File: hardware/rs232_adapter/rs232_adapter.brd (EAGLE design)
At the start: 53.3 x 36.5 mm, 9 parts, among them IC1 MAX202ECWE

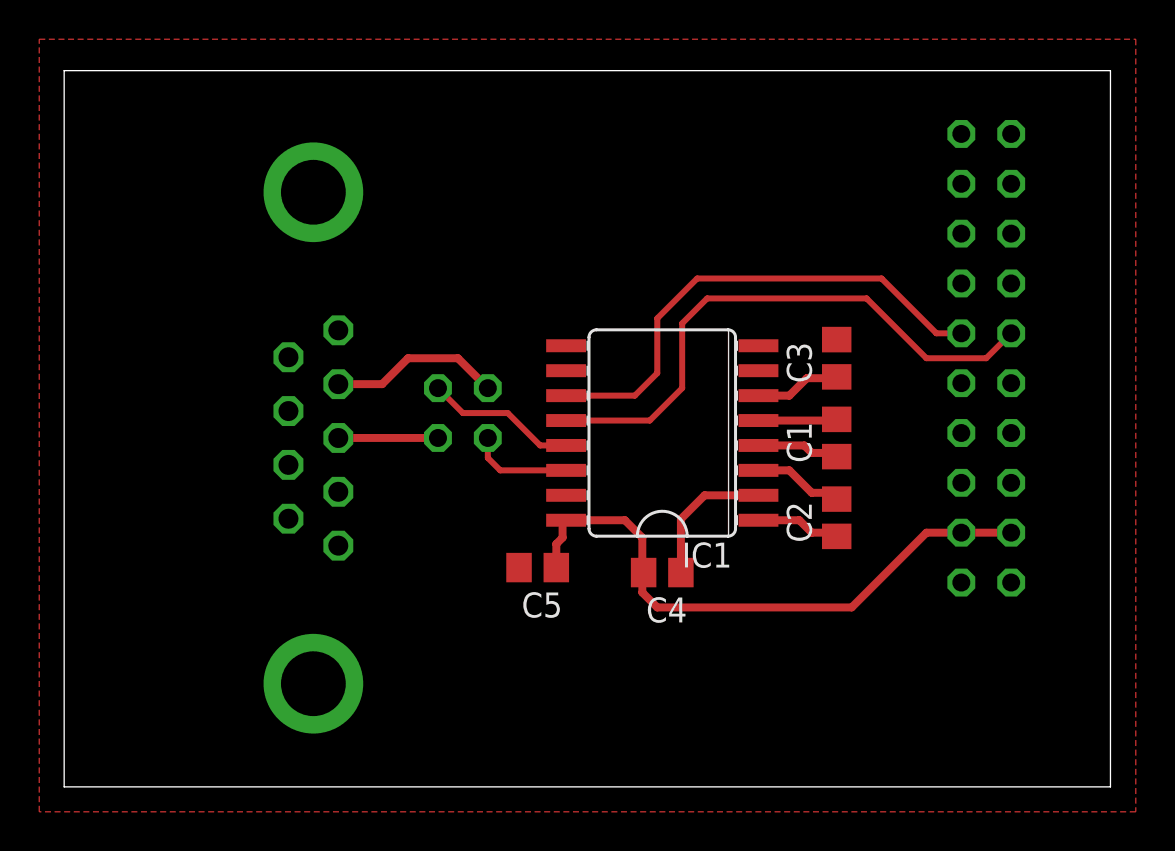
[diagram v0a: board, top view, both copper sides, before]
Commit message: change the package of the max202 and add some documentation
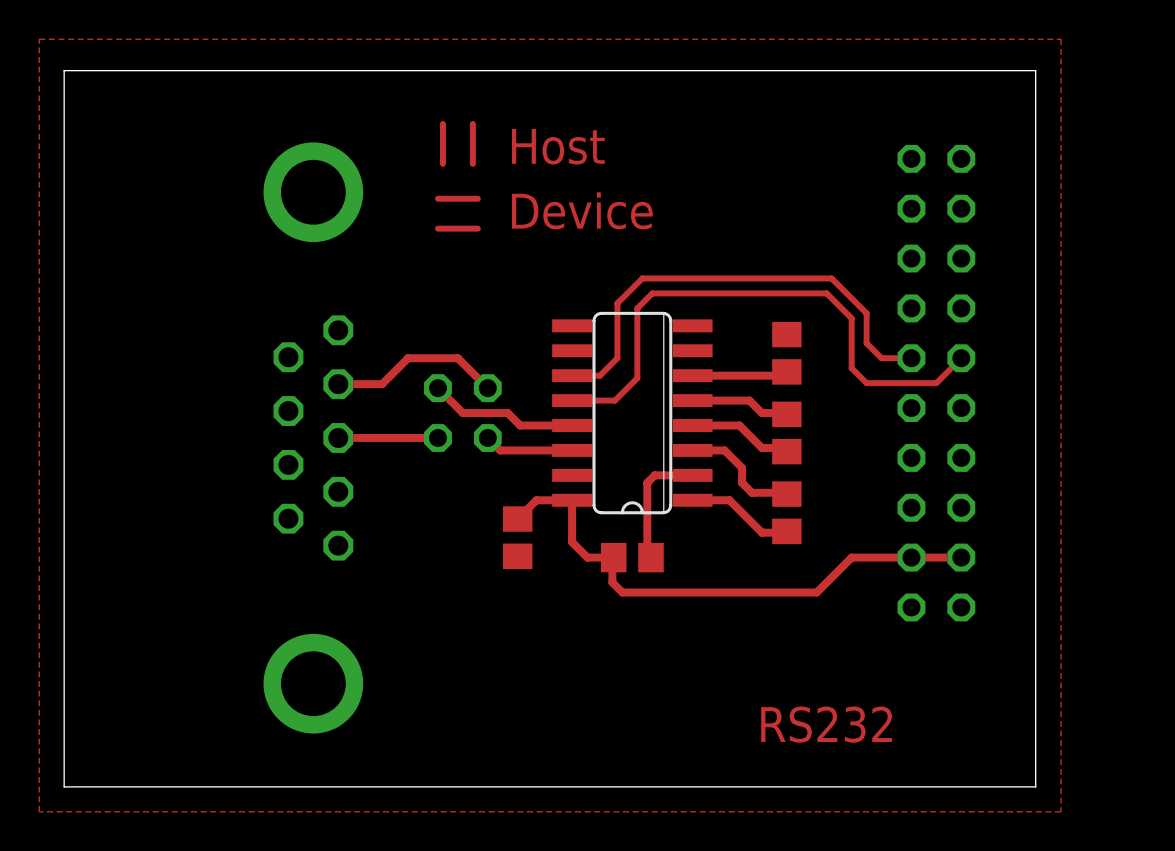
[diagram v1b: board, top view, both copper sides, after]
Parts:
- IC1: value MAX202ECWE -> MAX202ECWESMALL; device maxim:SO16L -> maxim:SO16
- moved SV2 2.84 mm to (44.5, 20.6)
- moved C1 2.55 mm to (36.8, 18.0)
- moved C2 2.55 mm to (36.8, 14.0)
- moved C3 2.55 mm to (36.8, 22.1)
- moved IC1 1.83 mm to (29.0, 19.1)
- moved C5 1.83 mm to (23.1, 12.7), turned to 270 degrees
- moved C4 1.70 mm to (29.0, 11.7)
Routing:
- net +5V: track 30.4 -> 27.8 mm
- net N$14: track 0.00 -> 2.03 mm
- net N$13: track 0.00 -> 2.03 mm
- net N$12: track 0.00 -> 2.03 mm
- net N$11: track 0.00 -> 2.03 mm
- net TX: track 25.4 -> 23.6 mm
- net N$3: track 4.59 -> 6.17 mm
- net N$4: track 4.33 -> 5.51 mm
- net N$2: track 4.22 -> 5.35 mm
- net N$1: track 4.01 -> 5.09 mm
- net RX: track 29.0 -> 28.1 mm
- net N$6: track 7.18 -> 6.36 mm
- net N$7: track 5.27 -> 4.56 mm
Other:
- board size 53.3 x 36.5 mm -> 49.5 x 36.5 mm
- board text added: "Device"
- board text added: "Host"
- board text added: "RS232"
